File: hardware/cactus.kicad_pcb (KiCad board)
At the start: 2 copper layers, 76.5 x 38.1 mm, 24 parts, among them SW1 SW_Push, U1 WeMos_Battery_Shield, U2 WeMos_D1_mini, U3 74HC595, U4 Si7021_breakout

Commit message: [mech] Change mounting hole diameter to 2mm
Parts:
- added REF**: MountingHole_2.2mm_M2, MountingHole:MountingHole_2.2mm_M2, F.Cu at (185.7, 80.5)
- REF** (x3): value MountingHole_3mm -> MountingHole_2.2mm_M2; footprint MountingHole:MountingHole_3mm -> MountingHole:MountingHole_2.2mm_M2
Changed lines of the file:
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@@
     (tracks 179)
     (zones 0)
-    (modules 24)
+    (modules 25)
     (nets 26)
   )
   (page A4)
   (layers
-    (0 F.Cu signal)
-    (31 B.Cu signal)
+    (0 F.Cu signal hide)
+    (31 B.Cu signal hide)
     (32 B.Adhes user)
     (33 F.Adhes user)
@@
     (add_net GND)
     (add_net VCC)
+  )
+  (module MountingHole:MountingHole_2.2mm_M2 (layer F.Cu)
+    (at 185.674 80.518)
+    (descr "Mounting Hole 2.2mm, no annular, M2")
+    (tags "mounting hole 2.2mm no annular m2")
+    (attr virtual)
+    (fp_text reference REF** (at 0 -3.2) (layer F.SilkS) hide
+      (effects (font (size 1 1) (thickness 0.15)))
+    )
+    (fp_text value MountingHole_2.2mm_M2 (at 0 3.2) (layer F.Fab)
+      (effects (font (size 1 1) (thickness 0.15)))
+    )
+    (fp_text user %R (at 0.3 0) (layer F.Fab)
+      (effects (font (size 1 1) (thickness 0.15)))
+    )
+    (fp_circle (center 0 0) (end 2.2 0) (layer Cmts.User) (width 0.15))
+    (fp_circle (center 0 0) (end 2.45 0) (layer F.CrtYd) (width 0.05))
+    (pad 1 np_thru_hole circle (at 0 0) (size 2.2 2.2) (drill 2.2) (layers *.Cu *.Mask))
+  )
+  (module MountingHole:MountingHole_2.2mm_M2 (layer F.Cu)
+    (at 118.364 84.328)
+    (descr "Mounting Hole 2.2mm, no annular, M2")
+    (tags "mounting hole 2.2mm no annular m2")
+    (attr virtual)
+    (fp_text reference REF** (at 0 -3.2) (layer F.SilkS)
+      (effects (font (size 1 1) (thickness 0.15)))
+    )
+    (fp_text value MountingHole_2.2mm_M2 (at 0 3.2) (layer F.Fab)
+      (effects (font (size 1 1) (thickness 0.15)))
+    )
+    (fp_circle (center 0 0) (end 2.45 0) (layer F.CrtYd) (width 0.05))
+    (fp_circle (center 0 0) (end 2.2 0) (layer Cmts.User) (width 0.15))
+    (fp_text user %R (at 0.3 0) (layer F.Fab)
+      (effects (font (size 1 1) (thickness 0.15)))
+    )
+    (pad 1 np_thru_hole circle (at 0 0) (size 2.2 2.2) (drill 2.2) (layers *.Cu *.Mask))
+  )
+  (module MountingHole:MountingHole_2.2mm_M2 (layer F.Cu)
+    (at 118.364 55.372)
+    (descr "Mounting Hole 2.2mm, no annular, M2")
+    (tags "mounting hole 2.2mm no annular m2")
+    (attr virtual)
+    (fp_text reference REF** (at 0 -3.2) (layer F.SilkS)
+      (effects (font (size 1 1) (thickness 0.15)))
+    )
+    (fp_text value MountingHole_2.2mm_M2 (at 0 3.2) (layer F.Fab)
+      (effects (font (size 1 1) (thickness 0.15)))
+    )
+    (fp_circle (center 0 0) (end 2.45 0) (layer F.CrtYd) (width 0.05))
+    (fp_circle (center 0 0) (end 2.2 0) (layer Cmts.User) (width 0.15))
+    (fp_text user %R (at 0.3 0) (layer F.Fab)
+      (effects (font (size 1 1) (thickness 0.15)))
+    )
+    (pad 1 np_thru_hole circle (at 0 0) (size 2.2 2.2) (drill 2.2) (layers *.Cu *.Mask))
+  )
+  (module MountingHole:MountingHole_2.2mm_M2 (layer F.Cu)
+    (at 185.674 55.372)
+    (descr "Mounting Hole 2.2mm, no annular, M2")
+    (tags "mounting hole 2.2mm no annular m2")
+    (attr virtual)
+    (fp_text reference REF** (at 0 -3.2) (layer F.SilkS)
+      (effects (font (size 1 1) (thickness 0.15)))
+    )
+    (fp_text value MountingHole_2.2mm_M2 (at 0 3.2) (layer F.Fab)
+      (effects (font (size 1 1) (thickness 0.15)))
+    )
+    (fp_circle (center 0 0) (end 2.45 0) (layer F.CrtYd) (width 0.05))
+    (fp_circle (center 0 0) (end 2.2 0) (layer Cmts.User) (width 0.15))
+    (fp_text user %R (at 0.3 0) (layer F.Fab)
+      (effects (font (size 1 1) (thickness 0.15)))
+    )
+    (pad 1 np_thru_hole circle (at 0 0) (size 2.2 2.2) (drill 2.2) (layers *.Cu *.Mask))
   )
   (module Symbol:OSHW-Logo2_7.3x6mm_SilkScreen (layer B.Cu)
@@
     (pad 8 thru_hole circle (at 11.049 -8.4455 180) (size 1.8 1.8) (drill 1.016) (layers *.Cu *.Mask B.SilkS))
   )
-  (module MountingHole:MountingHole_3mm (layer F.Cu)
-    (at 118.364 84.328)
-    (descr "Mounting Hole 3mm, no annular")
-    (tags "mounting hole 3mm no annular")
-    (attr virtual)
-    (fp_text reference REF** (at 4.064 0) (layer F.SilkS) hide
-      (effects (font (size 1 1) (thickness 0.15)))
-    )
-    (fp_text value MountingHole_3mm (at 0 4) (layer F.Fab)
-      (effects (font (size 1 1) (thickness 0.15)))
-    )
-    (fp_text user %R (at 0.3 0) (layer F.Fab)
-      (effects (font (size 1 1) (thickness 0.15)))
-    )
-    (fp_circle (center 0 0) (end 3 0) (layer Cmts.User) (width 0.15))
-    (fp_circle (center 0 0) (end 3.25 0) (layer F.CrtYd) (width 0.05))
-    (pad 1 np_thru_hole circle (at 0 0) (size 3 3) (drill 3) (layers *.Cu *.Mask))
-  )
-  (module MountingHole:MountingHole_3mm (layer F.Cu)
-    (at 118.364 55.372)
-    (descr "Mounting Hole 3mm, no annular")
-    (tags "mounting hole 3mm no annular")
-    (attr virtual)
-    (fp_text reference REF** (at 2.794 -3.81) (layer F.SilkS) hide
-      (effects (font (size 1 1) (thickness 0.15)))
-    )
-    (fp_text value MountingHole_3mm (at 0 4) (layer F.Fab)
-      (effects (font (size 1 1) (thickness 0.15)))
-    )
-    (fp_text user %R (at 0.3 0) (layer F.Fab)
-      (effects (font (size 1 1) (thickness 0.15)))
-    )
-    (fp_circle (center 0 0) (end 3 0) (layer Cmts.User) (width 0.15))
-    (fp_circle (center 0 0) (end 3.25 0) (layer F.CrtYd) (width 0.05))
-    (pad 1 np_thru_hole circle (at 0 0) (size 3 3) (drill 3) (layers *.Cu *.Mask))
-  )
   (module Si7021:Si7021_breakout_board (layer F.Cu)
     (at 179.832 79.248)
@@
     )
   )
-  (module MountingHole:MountingHole_3mm (layer F.Cu)
-    (at 185.674 55.372)
-    (descr "Mounting Hole 3mm, no annular")
-    (tags "mounting hole 3mm no annular")
-    (attr virtual)
-    (fp_text reference REF** (at 0 -4) (layer F.SilkS) hide
-      (effects (font (size 1 1) (thickness 0.15)))
-    )
-    (fp_text value MountingHole_3mm (at 0 4) (layer F.Fab)
-      (effects (font (size 1 1) (thickness 0.15)))
-    )
-    (fp_circle (center 0 0) (end 3.25 0) (layer F.CrtYd) (width 0.05))
-    (fp_circle (center 0 0) (end 3 0) (layer Cmts.User) (width 0.15))
-    (fp_text user %R (at 0.3 0) (layer F.Fab)
-      (effects (font (size 1 1) (thickness 0.15)))
-    )
-    (pad 1 np_thru_hole circle (at 0 0) (size 3 3) (drill 3) (layers *.Cu *.Mask))
-  )
-  (dimension 3.2004 (width 0.3) (layer Dwgs.User)
-    (gr_text "3.200 mm" (at 118.3386 93.921) (layer Dwgs.User)
-      (effects (font (size 1.5 1.5) (thickness 0.3)))
-    )
-    (feature1 (pts (xy 116.7384 84.4296) (xy 116.7384 92.407421)))
-    (feature2 (pts (xy 119.9388 84.4296) (xy 119.9388 92.407421)))
-    (crossbar (pts (xy 119.9388 91.821) (xy 116.7384 91.821)))
-    (arrow1a (pts (xy 116.7384 91.821) (xy 117.864904 91.234579)))
-    (arrow1b (pts (xy 116.7384 91.821) (xy 117.864904 92.407421)))
-    (arrow2a (pts (xy 119.9388 91.821) (xy 118.812296 91.234579)))
-    (arrow2b (pts (xy 119.9388 91.821) (xy 118.812296 92.407421)))
-  )
-  (dimension 38.2524 (width 0.3) (layer Dwgs.User)
+  (dimension 2.209946 (width 0.1) (layer Dwgs.User)
+    (gr_text "2.210 mm" (at 118.31136 92.184282 -0.6585431776) (layer Dwgs.User)
+      (effects (font (size 1 1) (thickness 0.1)))
+    )
+    (feature1 (pts (xy 117.2972 84.2772) (xy 117.223856 90.658103)))
+    (feature2 (pts (xy 119.507 84.3026) (xy 119.433656 90.683503)))
+    (crossbar (pts (xy 119.440396 90.097121) (xy 117.230596 90.071721)))
+    (arrow1a (pts (xy 117.230596 90.071721) (xy 118.363765 89.498286)))
+    (arrow1b (pts (xy 117.230596 90.071721) (xy 118.350285 90.67105)))
+    (arrow2a (pts (xy 119.440396 90.097121) (xy 118.320707 89.497792)))
+    (arrow2b (pts (xy 119.440396 90.097121) (xy 118.307227 90.670556)))
+  )
+  (dimension 38.2524 (width 0.1) (layer Dwgs.User)
     (gr_text "38.252 mm" (at 195.2162 69.9008 90) (layer Dwgs.User)
-      (effects (font (size 1.5 1.5) (thickness 0.3)))
+      (effects (font (size 1 1) (thickness 0.1)))
     )
     (feature1 (pts (xy 184.404 50.7746) (xy 193.702621 50.7746)))
@@
     (arrow2b (pts (xy 193.1162 89.027) (xy 192.529779 87.900496)))
   )
-  (dimension 76.174617 (width 0.3) (layer Dwgs.User)
+  (dimension 76.174617 (width 0.1) (layer Dwgs.User)
     (gr_text "76.175 mm" (at 152.152016 46.897333 0.03820991732) (layer Dwgs.User)
-      (effects (font (size 1.5 1.5) (thickness 0.3)))
+      (effects (font (size 1 1) (thickness 0.1)))
     )
     (feature1 (pts (xy 114.0714 56.9468) (xy 114.065724 48.436312)))

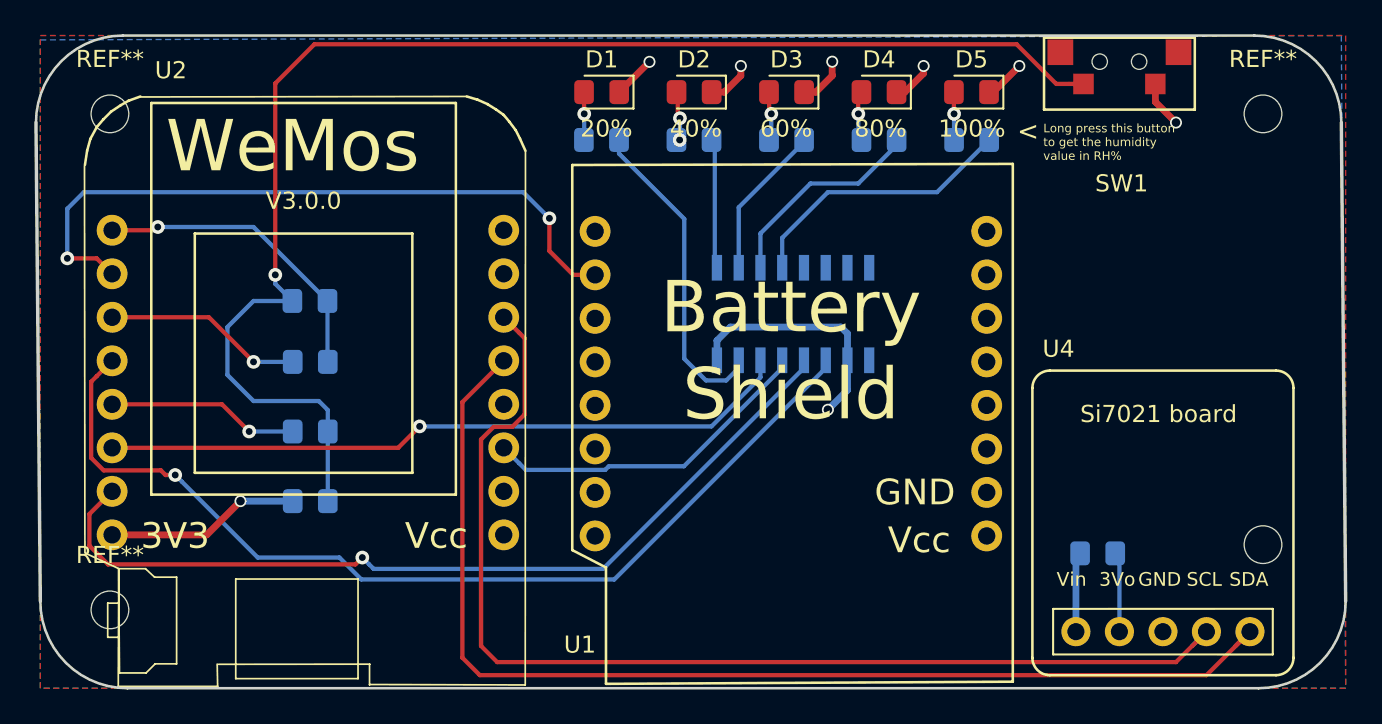
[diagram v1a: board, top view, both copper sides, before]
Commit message: [bom] Add order date for BOM
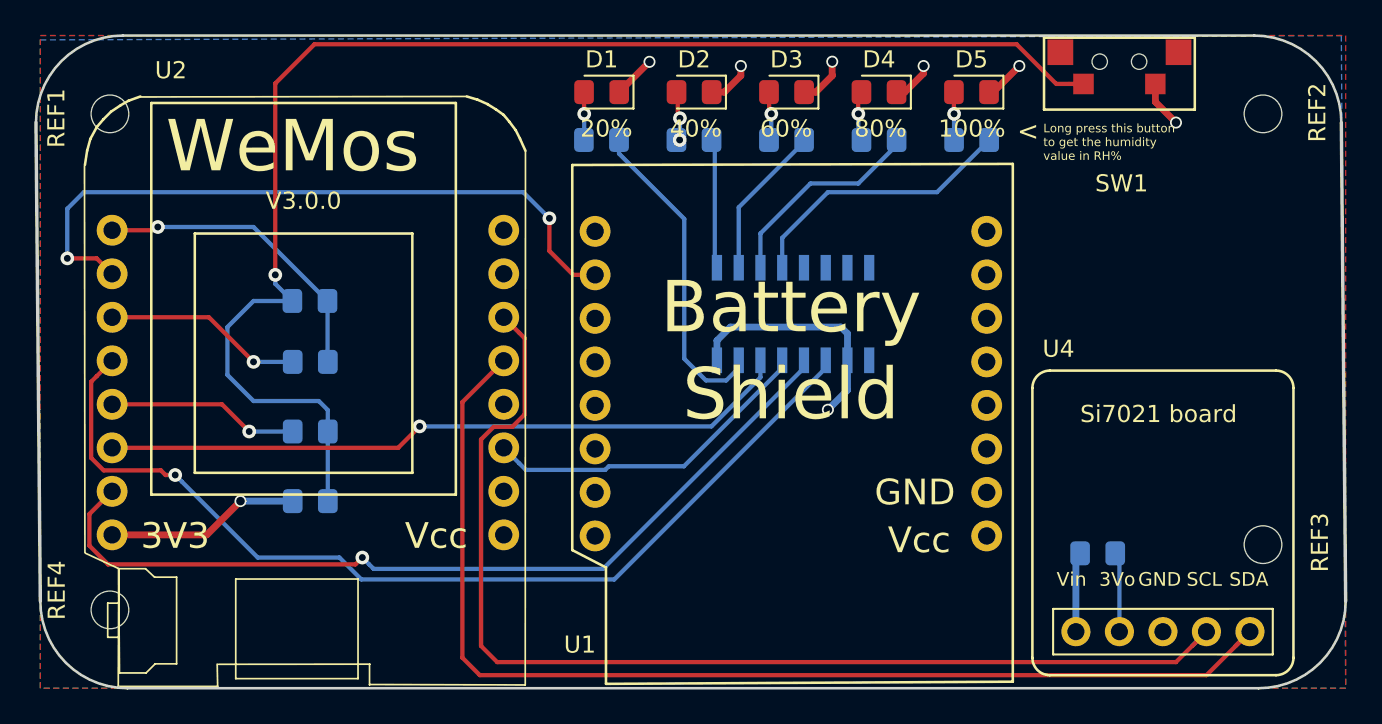
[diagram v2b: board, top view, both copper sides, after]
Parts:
- renumbered REF** to REF1, REF** to REF2, REF** to REF3, REF** to REF4
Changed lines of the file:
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@@
     (tags "mounting hole 2.2mm no annular m2")
     (attr virtual)
-    (fp_text reference REF** (at 0 -3.2) (layer F.SilkS) hide
+    (fp_text reference REF3 (at 3.3274 -0.127 90) (layer F.SilkS)
       (effects (font (size 1 1) (thickness 0.15)))
     )
-    (fp_text value MountingHole_2.2mm_M2 (at 0 3.2) (layer F.Fab)
-      (effects (font (size 1 1) (thickness 0.15)))
+    (fp_text value MountingHole_2.2mm_M2 (at 5.842 0.2032 90) (layer F.Fab)
+      (effects (font (size 0.8 0.8) (thickness 0.15)))
     )
     (fp_text user %R (at 0.3 0) (layer F.Fab)
@@
     (tags "mounting hole 2.2mm no annular m2")
     (attr virtual)
-    (fp_text reference REF** (at 0 -3.2) (layer F.SilkS)
+    (fp_text reference REF4 (at -3.0988 -1.143 90) (layer F.SilkS)
       (effects (font (size 1 1) (thickness 0.15)))
     )
-    (fp_text value MountingHole_2.2mm_M2 (at 0 3.2) (layer F.Fab)
-      (effects (font (size 1 1) (thickness 0.15)))
+    (fp_text value MountingHole_2.2mm_M2 (at -5.588 -2.6416 90) (layer F.Fab)
+      (effects (font (size 0.8 0.8) (thickness 0.15)))
     )
     (fp_circle (center 0 0) (end 2.45 0) (layer F.CrtYd) (width 0.05))
@@
     (tags "mounting hole 2.2mm no annular m2")
     (attr virtual)
-    (fp_text reference REF** (at 0 -3.2) (layer F.SilkS)
+    (fp_text reference REF1 (at -3.1242 0.254 90) (layer F.SilkS)
       (effects (font (size 1 1) (thickness 0.15)))
     )
-    (fp_text value MountingHole_2.2mm_M2 (at 0 3.2) (layer F.Fab)
-      (effects (font (size 1 1) (thickness 0.15)))
+    (fp_text value MountingHole_2.2mm_M2 (at -5.59425 1.9304 90) (layer F.Fab)
+      (effects (font (size 0.8 0.8) (thickness 0.125)))
     )
     (fp_circle (center 0 0) (end 2.45 0) (layer F.CrtYd) (width 0.05))
@@
     (tags "mounting hole 2.2mm no annular m2")
     (attr virtual)
-    (fp_text reference REF** (at 0 -3.2) (layer F.SilkS)
+    (fp_text reference REF2 (at 3.175 -0.0762 90) (layer F.SilkS)
       (effects (font (size 1 1) (thickness 0.15)))
     )
-    (fp_text value MountingHole_2.2mm_M2 (at 0 3.2) (layer F.Fab)
-      (effects (font (size 1 1) (thickness 0.15)))
+    (fp_text value MountingHole_2.2mm_M2 (at 5.842 3.2512 90) (layer F.Fab)
+      (effects (font (size 0.8 0.8) (thickness 0.15)))
     )
     (fp_circle (center 0 0) (end 2.45 0) (layer F.CrtYd) (width 0.05))

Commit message: [mech] Generate gerber
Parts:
- moved REF3 0.25 mm to (185.7, 80.3)
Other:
- board text added: "SW1"
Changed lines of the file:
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@@
   (general
     (thickness 1.6)
-    (drawings 35)
+    (drawings 36)
     (tracks 179)
     (zones 0)
@@
   (page A4)
   (layers
-    (0 F.Cu signal hide)
-    (31 B.Cu signal hide)
+    (0 F.Cu signal)
+    (31 B.Cu signal)
     (32 B.Adhes user)
     (33 F.Adhes user)
@@
     (visible_elements FEFFFEFF)
     (pcbplotparams
-      (layerselection 0x010fc_ffffffff)
+      (layerselection 0x0d0fc_ffffffff)
       (usegerberextensions false)
       (usegerberattributes false)
@@
       (outputformat 1)
       (mirror false)
-      (drillshape 1)
+      (drillshape 0)
       (scaleselection 1)
-      (outputdirectory ""))
+      (outputdirectory "/Users/sayanee/Documents/cactus/hardware/gerbers/"))
   )
   (net 0 "")
@@
   )
   (module MountingHole:MountingHole_2.2mm_M2 (layer F.Cu)
-    (at 185.674 80.518)
-    (descr "Mounting Hole 2.2mm, no annular, M2")
-    (tags "mounting hole 2.2mm no annular m2")
-    (attr virtual)
-    (fp_text reference REF3 (at 3.3274 -0.127 90) (layer F.SilkS)
-      (effects (font (size 1 1) (thickness 0.15)))
-    )
-    (fp_text value MountingHole_2.2mm_M2 (at 5.842 0.2032 90) (layer F.Fab)
-      (effects (font (size 0.8 0.8) (thickness 0.15)))
-    )
-    (fp_text user %R (at 0.3 0) (layer F.Fab)
-      (effects (font (size 1 1) (thickness 0.15)))
-    )
-    (fp_circle (center 0 0) (end 2.2 0) (layer Cmts.User) (width 0.15))
-    (fp_circle (center 0 0) (end 2.45 0) (layer F.CrtYd) (width 0.05))
-    (pad 1 np_thru_hole circle (at 0 0) (size 2.2 2.2) (drill 2.2) (layers *.Cu *.Mask))
-  )
-  (module MountingHole:MountingHole_2.2mm_M2 (layer F.Cu)
     (at 118.364 84.328)
     (descr "Mounting Hole 2.2mm, no annular, M2")
     (tags "mounting hole 2.2mm no annular m2")
     (attr virtual)
-    (fp_text reference REF4 (at -3.0988 -1.143 90) (layer F.SilkS)
-      (effects (font (size 1 1) (thickness 0.15)))
+    (fp_text reference REF4 (at -2.921 0 90) (layer F.SilkS)
+      (effects (font (size 0.8 0.8) (thickness 0.1)))
     )
     (fp_text value MountingHole_2.2mm_M2 (at -5.588 -2.6416 90) (layer F.Fab)
@@
     (tags "mounting hole 2.2mm no annular m2")
     (attr virtual)
-    (fp_text reference REF1 (at -3.1242 0.254 90) (layer F.SilkS)
-      (effects (font (size 1 1) (thickness 0.15)))
+    (fp_text reference REF1 (at -3.048 0 90) (layer F.SilkS)
+      (effects (font (size 0.8 0.8) (thickness 0.1)))
     )
     (fp_text value MountingHole_2.2mm_M2 (at -5.59425 1.9304 90) (layer F.Fab)
@@
     (tags "mounting hole 2.2mm no annular m2")
     (attr virtual)
-    (fp_text reference REF2 (at 3.175 -0.0762 90) (layer F.SilkS)
-      (effects (font (size 1 1) (thickness 0.15)))
+    (fp_text reference REF2 (at 3.175 0 90) (layer F.SilkS)
+      (effects (font (size 0.8 0.8) (thickness 0.1)))
     )
     (fp_text value MountingHole_2.2mm_M2 (at 5.842 3.2512 90) (layer F.Fab)
@@
     (tags "Logo Symbol OSHW")
     (attr virtual)
-    (fp_text reference LOGO (at 6.096 0.127 180) (layer B.SilkS) hide
+    (fp_text reference LOGO (at 6.096 0.127 180) (layer B.Fab) hide
       (effects (font (size 1 1) (thickness 0.15)) (justify mirror))
     )
@@
     (fp_line (start 12.827 -15.621) (end 12.827 14.605) (layer F.SilkS) (width 0.15))
     (fp_line (start -12.8905 -15.5575) (end 12.827 -15.621) (layer F.SilkS) (width 0.15))
-    (fp_text user "WeMos Battery Shield" (at 0.254 12.954 180) (layer B.SilkS)
+    (fp_text user "WeMos Battery Shield" (at 0.7112 12.8778 180) (layer B.SilkS)
       (effects (font (size 1 1) (thickness 0.15)) (justify mirror))
     )
@@
     (fp_line (start -4.594931 17.728537) (end -4.594931 11.9148) (layer F.SilkS) (width 0.1))
     (fp_line (start 2.54465 17.728537) (end -4.594931 17.728537) (layer F.SilkS) (width 0.1))
-    (fp_text user "WeMos V3.0.0" (at -0.889 15.24 180) (layer B.SilkS)
+    (fp_text user "WeMos V3.0.0" (at 0.2794 13.8176 180) (layer B.SilkS)
       (effects (font (size 1 1) (thickness 0.15)) (justify mirror))
     )
@@
     (tags "resistor handsolder")
     (attr smd)
-    (fp_text reference R9 (at 0 -1.778) (layer B.SilkS)
+    (fp_text reference R9 (at 0.127 1.778) (layer B.SilkS)
       (effects (font (size 1 1) (thickness 0.15)) (justify mirror))
     )
@@
     )
   )
+  (module MountingHole:MountingHole_2.2mm_M2 (layer F.Cu)
+    (at 185.674 80.264)
+    (descr "Mounting Hole 2.2mm, no annular, M2")
+    (tags "mounting hole 2.2mm no annular m2")
+    (attr virtual)
+    (fp_text reference REF3 (at 3.048 0 90) (layer F.SilkS)
+      (effects (font (size 0.8 0.8) (thickness 0.1)))
+    )
+    (fp_text value MountingHole_2.2mm_M2 (at 5.969 -0.381 90) (layer F.Fab)
+      (effects (font (size 0.8 0.8) (thickness 0.15)))
+    )
+    (fp_circle (center 0 0) (end 2.45 0) (layer F.CrtYd) (width 0.05))
+    (fp_circle (center 0 0) (end 2.2 0) (layer Cmts.User) (width 0.15))
+    (fp_text user %R (at 3.302 -0.254 90) (layer F.Fab)
+      (effects (font (size 1 1) (thickness 0.15)))
+    )
+    (pad 1 np_thru_hole circle (at 0 0) (size 2.2 2.2) (drill 2.2) (layers *.Cu *.Mask))
+  )
+  (gr_text SW1 (at 177.3936 53.2384) (layer B.SilkS)
+    (effects (font (size 1 1) (thickness 0.1)) (justify mirror))
+  )
   (dimension 2.209946 (width 0.1) (layer Dwgs.User)
     (gr_text "2.210 mm" (at 118.31136 92.184282 -0.6585431776) (layer Dwgs.User)
@@
     (effects (font (size 1 1) (thickness 0.1)))
   )
-  (gr_text "Enable 4-pin\nSi7021 board" (at 184.404 81.026) (layer B.SilkS)
+  (gr_text "Enable 4-pin\nSi7021 board" (at 178.816 78.613) (layer B.SilkS)
     (effects (font (size 0.6 0.6) (thickness 0.1)) (justify left mirror))
   )
